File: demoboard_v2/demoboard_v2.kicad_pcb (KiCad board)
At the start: 2 copper layers, 0 parts

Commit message: Added 104 connector, put 104 footprint in PCB and have decoupling caps for the mcu.
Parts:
- added 1uF1: C, SFUSat:C_0402, F.Cu at (236.4, 57.8)
- added C1: 0.1µF, SFUSat:C_0402, F.Cu at (225.4, 63.9)
- added C10: 0.1µF, SFUSat:C_0402, F.Cu at (227.1, 74.4)
- added C11: 0.1µF, SFUSat:C_0402, F.Cu at (241.4, 63.0)
- added C12: 0.1µF, SFUSat:C_0402, F.Cu at (231.8, 73.4)
- added C13: 0.1µF, SFUSat:C_0402, F.Cu at (224.0, 79.6)
- added C14: 0.1µF, SFUSat:C_0402, F.Cu at (239.4, 68.2)
- added C15: 0.1µF, SFUSat:C_0402, F.Cu at (228.7, 79.6)
- added C16: 0.1µF, SFUSat:C_0402, F.Cu at (236.4, 73.4)
- added C17: 0.1µF, SFUSat:C_0402, F.Cu at (244.1, 68.2)
- added C18: 0.1µF, SFUSat:C_0402, F.Cu at (233.3, 78.7)
- added C19: 0.1µF, SFUSat:C_0402, F.Cu at (241.1, 73.4)
- added C2: 1uF, SFUSat:C_0402, F.Cu at (218.5, 73.0)
- added C20: 0.1µF, SFUSat:C_0402, F.Cu at (238.0, 78.7)
- added C3: 0.1µF, SFUSat:C_0402, F.Cu at (236.7, 63.0)
- added C4: 0.1µF, SFUSat:C_0402, F.Cu at (222.4, 73.0)
- added C5: 0.1µF, SFUSat:C_0402, F.Cu at (219.3, 78.2)
- added C6: 0.1µF, SFUSat:C_0402, F.Cu at (230.0, 63.9)
- added C7: 0.1µF, SFUSat:C_0402, F.Cu at (240.8, 57.8)
- added C8: 0.1µF, SFUSat:C_0402, F.Cu at (234.7, 68.2)
- added C9: 0.1µF, SFUSat:C_0402, F.Cu at (227.1, 69.1)
- added P1: POWER_IN_CONNECTOR, SFUSat:2x01In_Header_v2, F.Cu at (224.2, 57.8)
- added REF**: PC104PTH, SFUSat:PC104PTH, F.Cu at (108.3, 27.1)
- added REF**: PC104PTH, SFUSat:PC104PTH, F.Cu at (186.8, 26.8)
- added REF**: PC104PTH, SFUSat:PC104PTH, F.Cu at (107.8, 102.0)
- added REF**: PC104PTH, SFUSat:PC104PTH, F.Cu at (185.5, 98.0)
- added U1: TMS570LS0714, Housings_QFP:LQFP-144_20x20mm_Pitch0.5mm, F.Cu at (134.7, 63.6)
- added U2: AP7331, SFUSat:SOT25, F.Cu at (220.0, 65.5)
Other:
- board outline added: 95.9 x 90.2 mm

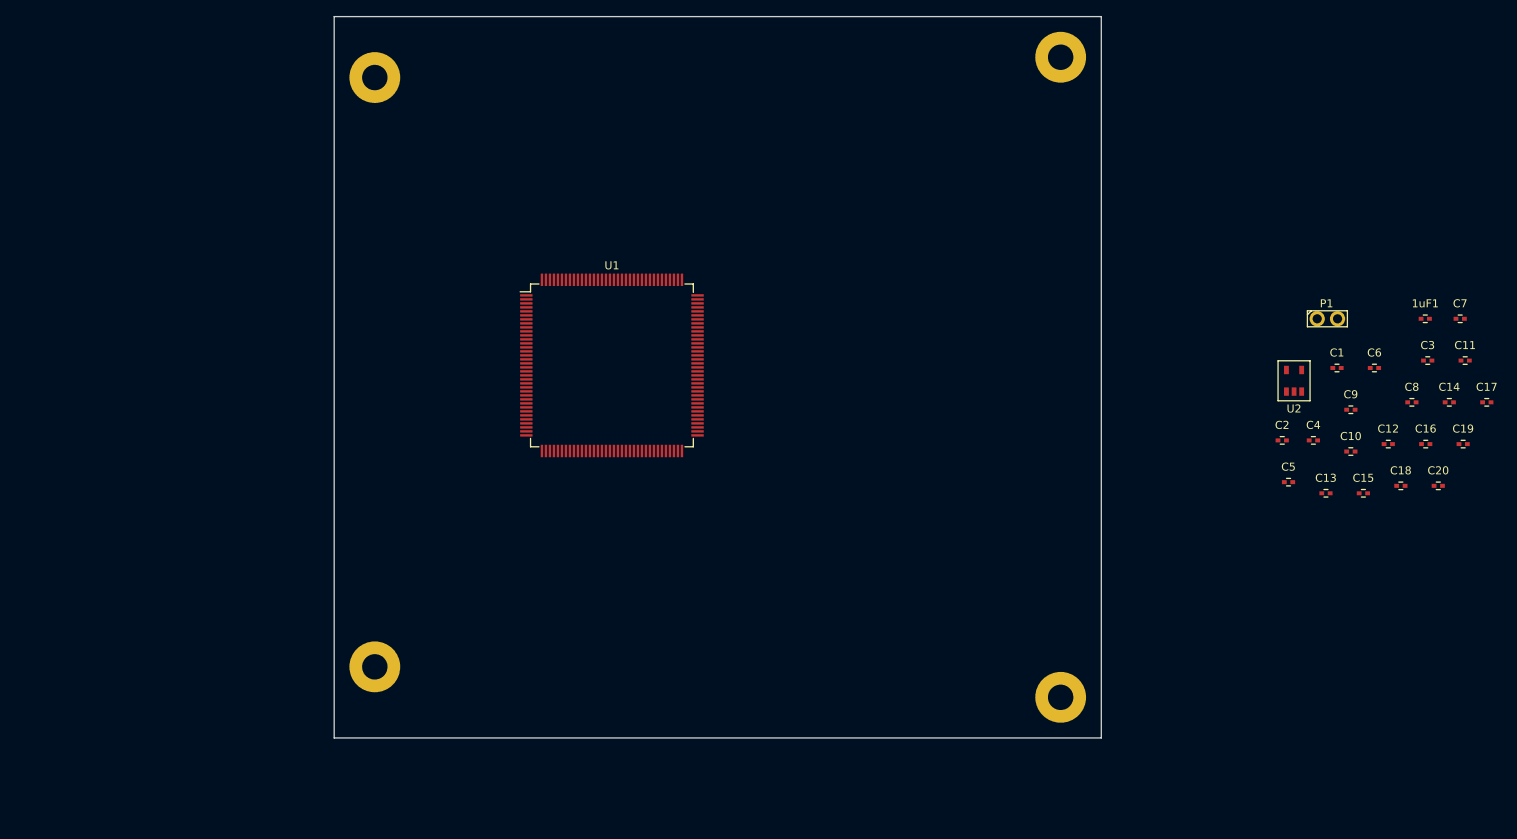
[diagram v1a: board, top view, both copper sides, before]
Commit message: Added RF SPI to schematic
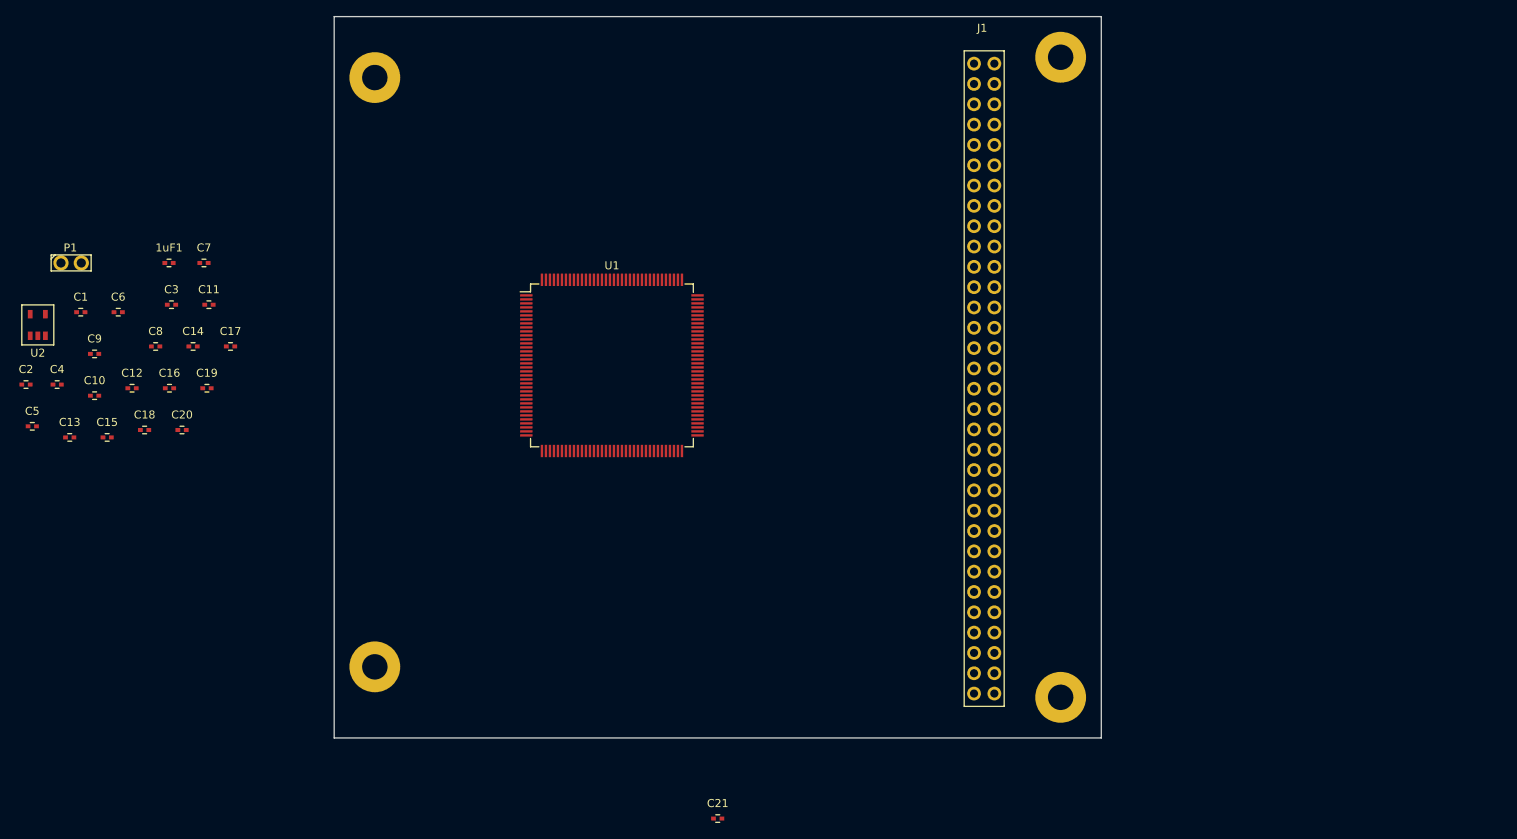
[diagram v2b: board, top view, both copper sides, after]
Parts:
- added C21: 1µF, SFUSat:C_0402, F.Cu at (147.9, 120.2)
- added J1: PC104-8BIT, SFUSat:PC104-8bit, F.Cu at (181.2, 65.2)
- moved C11 157.2 mm to (84.3, 56.0)
- moved C15 157.2 mm to (71.6, 72.6)
- moved C19 157.2 mm to (84.1, 66.5)
- moved C2 157.2 mm to (61.5, 66.0)
- moved C4 157.2 mm to (65.4, 66.0)
- moved C8 157.2 mm to (77.7, 61.2)
- moved C1 157.2 mm to (68.3, 56.9)
- moved C12 157.2 mm to (74.7, 66.5)
- moved C13 157.2 mm to (66.9, 72.6)
- moved C16 157.2 mm to (79.4, 66.5)
- moved C17 157.2 mm to (87.0, 61.2)
- moved C20 157.2 mm to (81.0, 71.7)
- moved C3 157.2 mm to (79.7, 56.0)
- moved C5 157.2 mm to (62.3, 71.2)
- moved C6 157.2 mm to (73.0, 56.9)
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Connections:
- U1 pad 100: (no net) -> Net-(U1-Pad100)
- U1 pad 105: (no net) -> Net-(U1-Pad105)
- U1 pad 106: (no net) -> Net-(U1-Pad106)
- U1 pad 130: (no net) -> Net-(U1-Pad130)
- U1 pad 23: (no net) -> Net-(U1-Pad23)
- U1 pad 24: (no net) -> Net-(U1-Pad24)
- U1 pad 25: (no net) -> Net-(U1-Pad25)
- U1 pad 30: (no net) -> Net-(U1-Pad30)
- U1 pad 31: (no net) -> Net-(U1-Pad31)
- U1 pad 32: (no net) -> Net-(U1-Pad32)
- U1 pad 37: (no net) -> RF_CS
- U1 pad 40: (no net) -> Net-(U1-Pad40)
- U1 pad 41: (no net) -> Net-(U1-Pad41)
- U1 pad 51: (no net) -> RF_MISO
- U1 pad 52: (no net) -> RF_MOSI
- U1 pad 53: (no net) -> RF_CLK
- U1 pad 54: (no net) -> Net-(U1-Pad54)
- U1 pad 6: (no net) -> RF_GAIN_CS
- U1 pad 91: (no net) -> Net-(U1-Pad91)
- U1 pad 93: (no net) -> Net-(U1-Pad93)
- U1 pad 94: (no net) -> Net-(U1-Pad94)
- U1 pad 95: (no net) -> Net-(U1-Pad95)
- U1 pad 96: (no net) -> Net-(U1-Pad96)
- U1 pad 97: (no net) -> Net-(U1-Pad97)
- U1 pad 98: (no net) -> Net-(U1-Pad98)
- U1 pad 99: (no net) -> Net-(U1-Pad99)

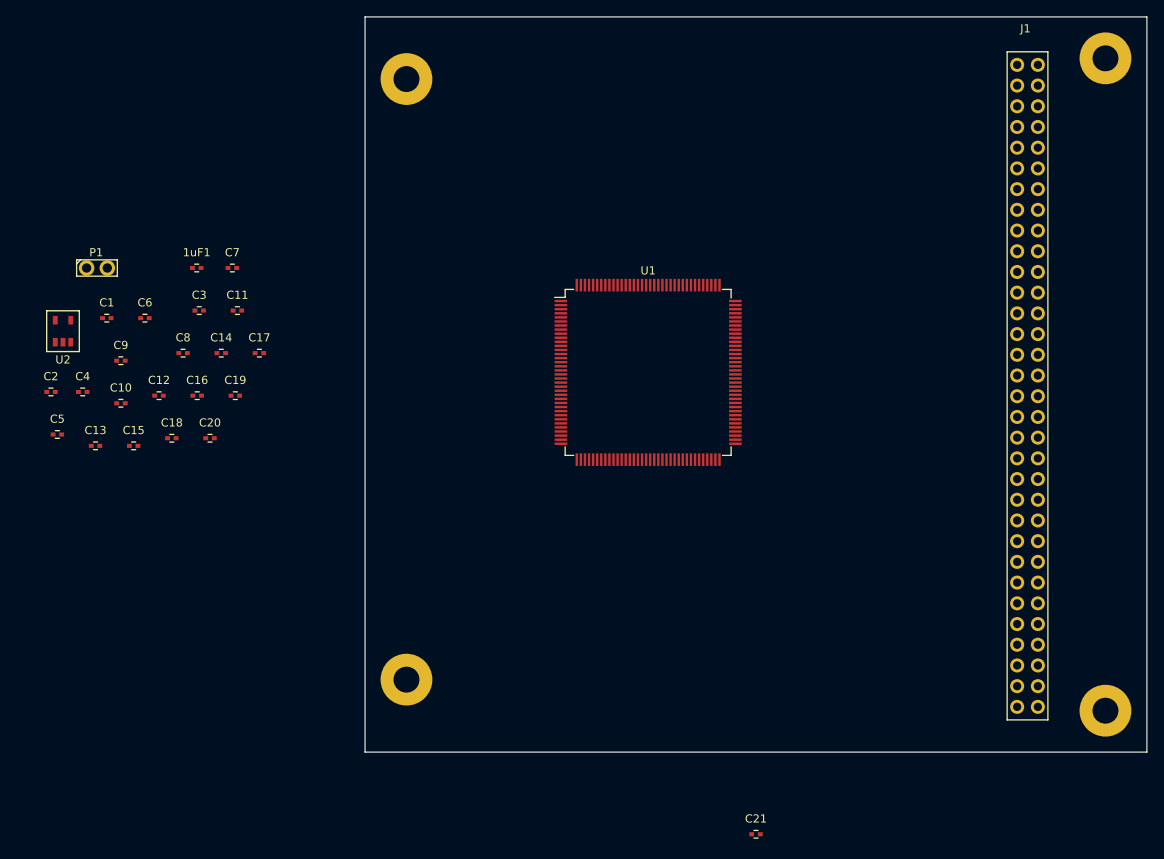
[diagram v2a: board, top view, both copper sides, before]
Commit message: Beginning to add latchup circuit. Latchup protection can be disabled with jumpers, and now has a current limit of 800mA
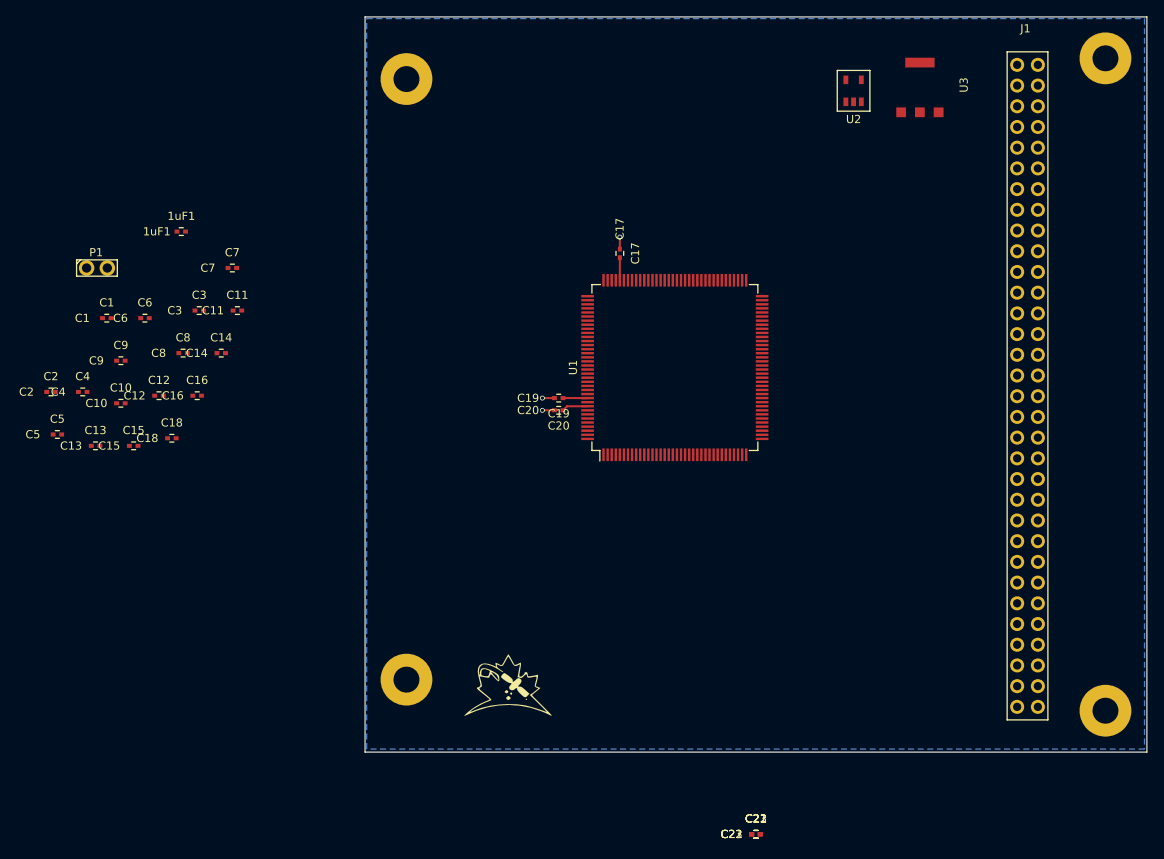
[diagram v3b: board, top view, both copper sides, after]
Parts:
- added C22: 4.7µF, SFUSat:C_0402, F.Cu at (147.9, 120.2)
- added C23: 1µF, SFUSat:C_0402, F.Cu at (147.9, 120.2)
- added G***: LOGO, SFUSat:SFUSat_15mm_2, F.Cu at (117.5, 102.0)
- added U3: AP7361_3.3v, SFUSat:SOT-223, F.Cu at (168.1, 28.6)
- P1: value POWER_IN_CONNECTOR -> 3v3_IN_CONNECTOR
- moved U2 101.4 mm to (159.9, 29.1)
- moved C17 45.9 mm to (131.2, 49.0), turned to 270 degrees
- moved C20 42.9 mm to (123.8, 68.2), turned to 180 degrees
- moved C19 39.7 mm to (123.8, 66.8), turned to 180 degrees
- moved 1uF1 4.85 mm to (77.5, 46.3)
- moved U1 3.33 mm to (138.0, 63.0), turned to 90 degrees
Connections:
- J1 pad 29B: Net-(J1-Pad29B) -> 5v0
- J1 pad 3B: Net-(J1-Pad3B) -> 5v0
- U1 pad 108: (no net) -> Net-(U1-Pad108)
- U1 pad 109: (no net) -> Net-(U1-Pad109)
- U1 pad 110: (no net) -> Net-(U1-Pad110)
- U1 pad 111: (no net) -> Net-(U1-Pad111)
- U1 pad 112: (no net) -> Net-(U1-Pad112)
- U1 pad 113: (no net) -> Net-(U1-Pad113)
- U1 pad 116: (no net) -> Net-(U1-Pad116)
- U1 pad 117: (no net) -> Net-(U1-Pad117)
- U1 pad 119: (no net) -> Net-(U1-Pad119)
- U1 pad 14: (no net) -> Net-(U1-Pad14)
- U1 pad 18: (no net) -> Net-(U1-Pad18)
- U1 pad 19: (no net) -> Net-(U1-Pad19)
- U1 pad 20: (no net) -> Net-(U1-Pad20)
- U1 pad 34: (no net) -> Net-(U1-Pad34)
- U1 pad 46: (no net) -> Net-(U1-Pad46)
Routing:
- net 3v3: track 0.00 -> 9.03 mm
- net GND: track 0.00 -> 4.42 mm, vias 0 -> 3
- added copper zone on B.Cu, net GND

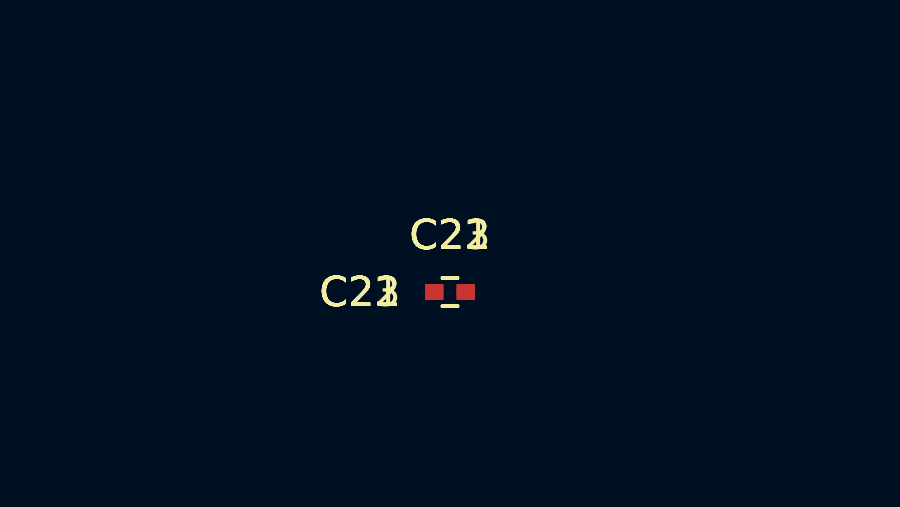
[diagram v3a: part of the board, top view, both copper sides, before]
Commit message: Completed power jumper setup for SEL monitor
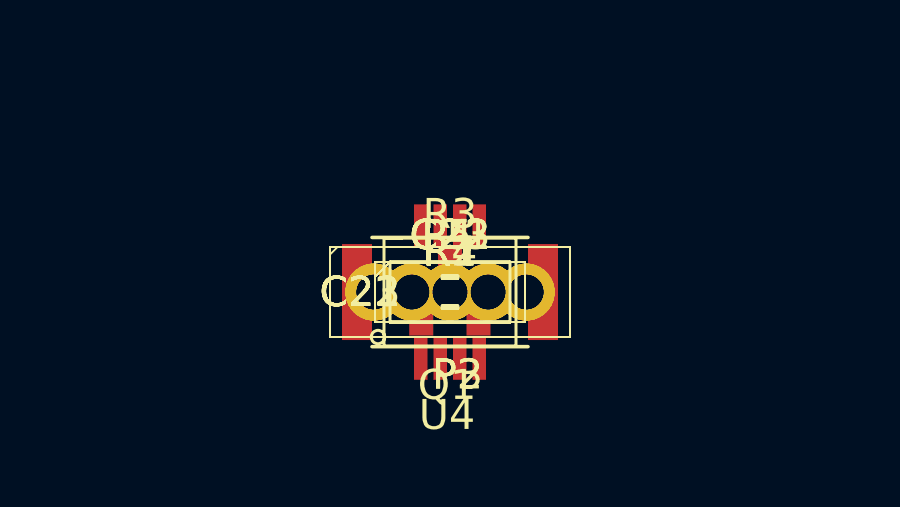
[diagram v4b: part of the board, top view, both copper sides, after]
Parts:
- added P2, P3: CONN_01X03, SFUSat:3x_01In_Header_v2, F.Cu at (147.9, 120.2)
- added P4, P5: CONN_01X02, SFUSat:2x01In_Header_v2, F.Cu at (147.9, 120.2)
- added Q1: DMN2075U, SFUSat:SOT23_DMN2075U, F.Cu at (147.9, 120.2)
- added R1: 2k, SFUSat:R_0402, F.Cu at (147.9, 120.2)
- added R2, R4: 10k, SFUSat:R_0402, F.Cu at (147.9, 120.2)
- added R3: 0.04, Resistors_SMD:R_2512, F.Cu at (147.9, 120.2)
- added U4: INA301, SFUSat:VSSOP_8, F.Cu at (147.9, 120.2)
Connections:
- net Net-(J1-Pad5A) renamed RF_IRQ
- C22 pad 1: 3v3 -> 3v3_OUTPUT
- C22 pad 2: GND -> 104_GND
- C23 pad 2: GND -> 104_GND
- J1 pad 1B: GND -> 104_GND
- J1 pad 31B: GND -> 104_GND
- J1 pad 32A: GND -> 104_GND
- J1 pad 32B: GND -> 104_GND
- U3 pad 2: GND -> 104_GND
- U3 pad 3: 3v3 -> 3v3_OUTPUT
- U3 pad 4: GND -> 104_GND

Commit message: 3v3 reverse polarity FET, connected current monitor to ADC, defined RF PWM and ADC pins on 104 connector, added UART connector, pc104 reverse polarity FET, 104 connector TVS diode.
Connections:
- J1 pad 22A: Net-(J1-Pad22A) -> (no net)
- J1 pad 23A: Net-(J1-Pad23A) -> (no net)
- J1 pad 24A: Net-(J1-Pad24A) -> (no net)
- J1 pad 25A: Net-(J1-Pad25A) -> (no net)
- J1 pad 26A: Net-(J1-Pad26A) -> (no net)
- J1 pad 27A: Net-(J1-Pad27A) -> (no net)
- J1 pad 28A: Net-(J1-Pad28A) -> (no net)
- J1 pad 29A: Net-(J1-Pad29A) -> (no net)
- J1 pad 30A: Net-(J1-Pad30A) -> (no net)
- J1 pad 31A: Net-(J1-Pad31A) -> (no net)
- J1 pad 32A: 104_GND -> (no net)
